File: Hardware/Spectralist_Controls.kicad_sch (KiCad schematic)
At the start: 30 parts, among them J1 Conn_01x8_Pin, J10 FilterA_CV, J11 FilterB_CV, J12 ChannelAOut, J13 ChannelBOut, J14 Conn_01x03_Pin, J15 Conn_01x02_Pin, J16 Conn_01x02_Pin, J2 Conn_01x8_Pin, J3 Conn_01x10_Pin, J4 Conn_01x10_Pin, J5 StretchCV, J6 VOctCV, J7 WarpCV, J8 PanCV, J9 SlopeCV, SW1 Harmonic_Switch, SW2 Filter_Switch, SW3 B_Octave

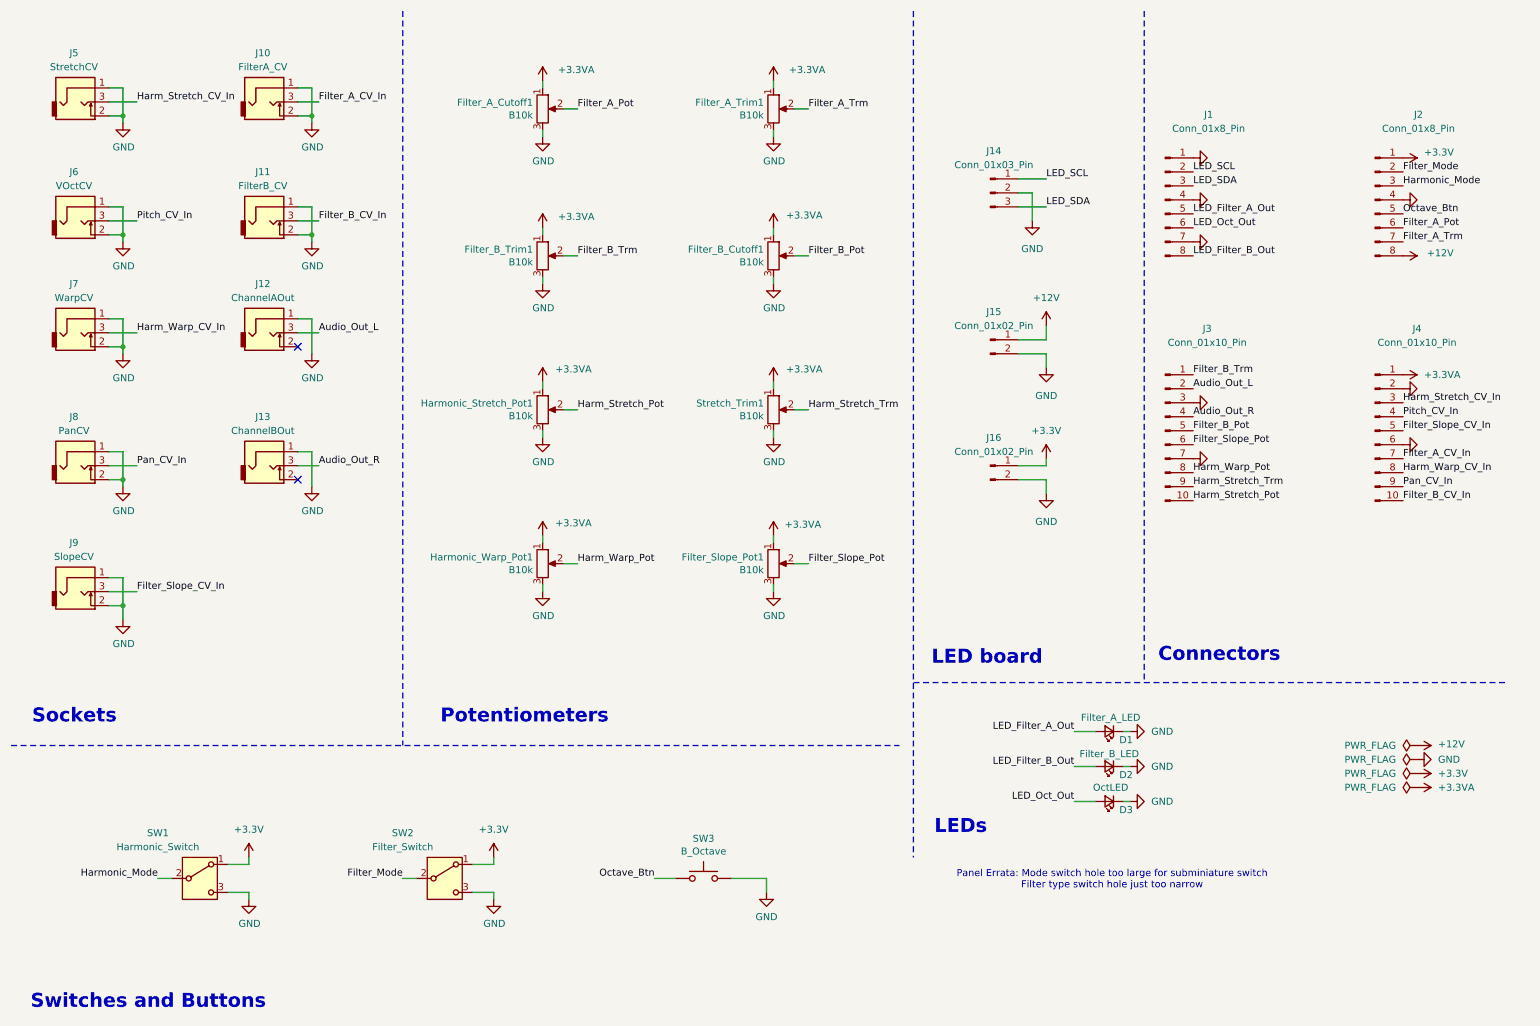
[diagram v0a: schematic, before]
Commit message: Code tidy up; implementing CV , pots and trimmers
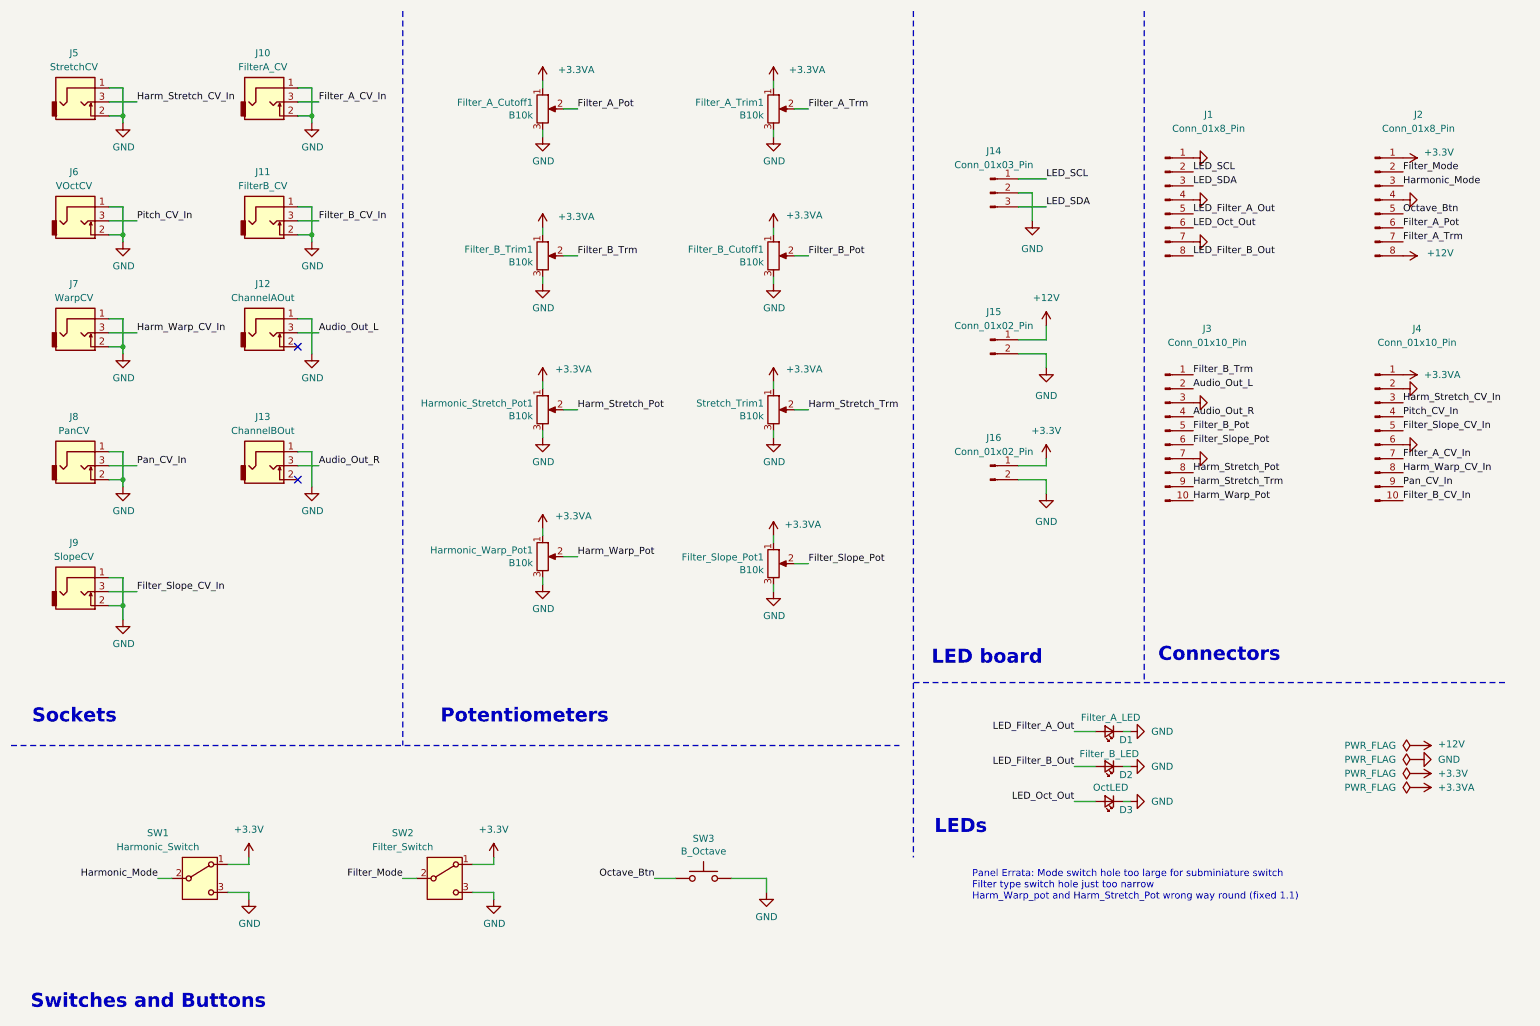
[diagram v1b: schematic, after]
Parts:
- renumbered Harmonic_Warp_Pot1 to Harmonic_Stretch_Pot1, Harmonic_Stretch_Pot1 to Harmonic_Warp_Pot1
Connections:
- net Harm_Stretch_Pot: now also Harmonic_Stretch_Pot1.2, J3.8 (Pin_8); no longer Harmonic_Warp_Pot1.2, J3.10 (Pin_10)
- net Harm_Warp_Pot: now also Harmonic_Warp_Pot1.2, J3.10 (Pin_10); no longer Harmonic_Stretch_Pot1.2, J3.8 (Pin_8)
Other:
- note added: "Panel Errata: Mode switch hole too large for subminiature switch Filter type switch hole just too narrow Harm_Warp_pot and Harm_Stretch_Pot wrong way round (fixed 1.1)"
- note removed: "Panel Errata: Mode switch hole too large for subminiature switch Filter type switch hole just too narrow"
- title: Kishoof Components -> Kishoof Controls
- moved on the sheet: Harmonic_Stretch_Pot1, Harmonic_Warp_Pot1
